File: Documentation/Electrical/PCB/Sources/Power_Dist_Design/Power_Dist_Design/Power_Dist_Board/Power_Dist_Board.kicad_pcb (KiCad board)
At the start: 2 copper layers, 150.5 x 84.8 mm, 59 parts, among them J1 Battery Connector, J2 +5V, J3 +5V, J4 +3.3V, J5 +3.3V, J6 GND, J7 GND, M1 Motor_DC, M10 Motor_DC, M2 Motor_DC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

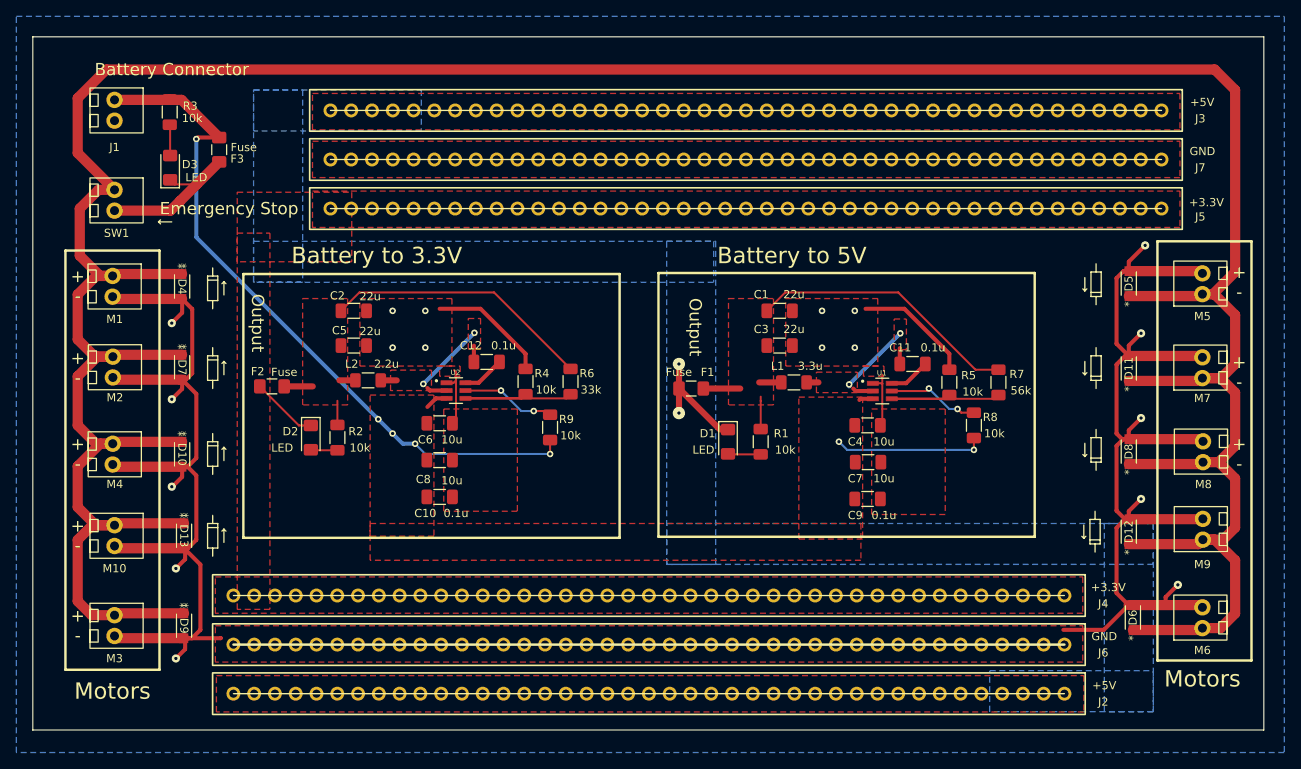
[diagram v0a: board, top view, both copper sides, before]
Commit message: Made final edits to pcb for ground isolation and EMI mitigation
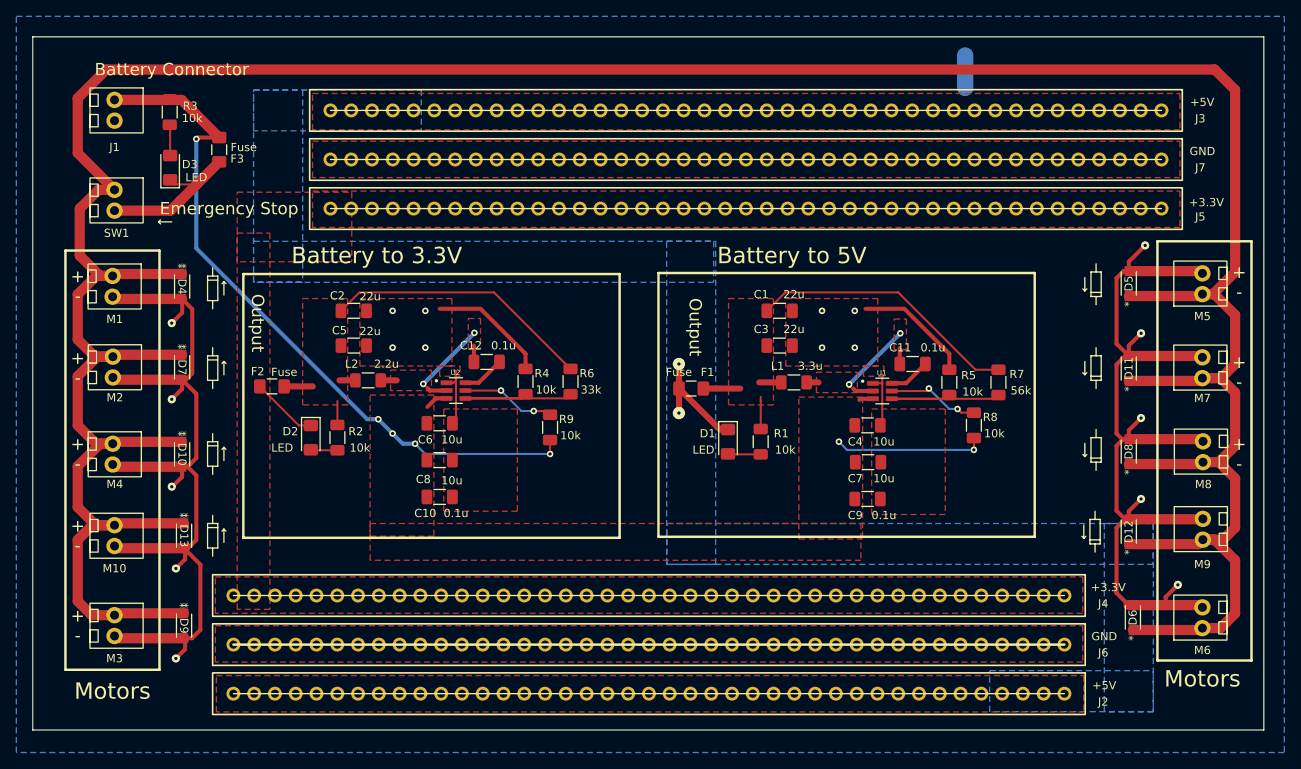
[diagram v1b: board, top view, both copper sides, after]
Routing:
- net GND: track 273.5 -> 264.3 mm
- net /vin: track 108.4 -> 109.2 mm
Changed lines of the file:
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@@
   )
   (dimension (type aligned) (layer "Eco1.User")
-    (pts (xy 239.5 20) (xy 239.5 104.5))
+    (pts (xy 235.75 20) (xy 235.75 104.5))
     (height -5.5)
-    (gr_text "3.3268 in" (at 243.85 62.25 90) (layer "Eco1.User")
+    (gr_text "84.5000 mm" (at 240.1 62.25 90) (layer "Eco1.User")
       (effects (font (size 1 1) (thickness 0.15)))
     )
@@
   )
   (dimension (type aligned) (layer "Eco1.User")
-    (pts (xy 82 113.5) (xy 232.5 113.5))
+    (pts (xy 82 108.25) (xy 232.5 108.25))
     (height 5)
-    (gr_text "5.9252 in" (at 157.25 117.35) (layer "Eco1.User")
+    (gr_text "150.5000 mm" (at 157.25 112.1) (layer "Eco1.User")
       (effects (font (size 1 1) (thickness 0.15)))
     )
@@
   (segment (start 214.5 60.065696) (end 215.544846 59.02085) (width 0.5) (layer "F.Cu") (net 2))
   (segment (start 100.633 93.633) (end 100.633 94.867) (width 0.5) (layer "F.Cu") (net 2))
-  (segment (start 215.976 89.476) (end 212.952 92.5) (width 0.5) (layer "F.Cu") (net 2))
-  (segment (start 212.952 92.5) (end 208 92.5) (width 0.5) (layer "F.Cu") (net 2))
   (segment (start 215.35375 48.64625) (end 216 48.64625) (width 0.5) (layer "F.Cu") (net 2))
   (segment (start 100.9375 72.5625) (end 102 73.625) (width 0.5) (layer "F.Cu") (net 2))
@@
   (segment (start 215.976 89.476) (end 214.5 88) (width 0.5) (layer "F.Cu") (net 2))
   (segment (start 100.633 83.867) (end 99.367 85.133) (width 0.5) (layer "F.Cu") (net 2))
-  (segment (start 101.024 93.524) (end 104.976 93.524) (width 0.5) (layer "F.Cu") (net 2))
   (segment (start 92.04 52.048) (end 91.766 51.774) (width 1.25) (layer "F.Cu") (net 2))
   (segment (start 184.7075 62.35375) (end 185.8125 62.35375) (width 0.25) (layer "F.Cu") (net 2))
-  (segment (start 104.976 93.524) (end 105 93.5) (width 0.5) (layer "F.Cu") (net 2))
   (segment (start 100.976 82.524) (end 100.5 82.524) (width 0.5) (layer "F.Cu") (net 2))
   (segment (start 100.9375 72.5625) (end 102 71.5) (width 0.5) (layer "F.Cu") (net 2))
@@
   (via (at 99.5 96) (size 1) (drill 0.4) (layers "F.Cu" "B.Cu") (net 2))
   (via (at 178.5 58) (size 0.8) (drill 0.4) (layers "F.Cu" "B.Cu") (free) (net 2))
+  (segment (start 196 22.28) (end 196 26.25) (width 2) (layer "B.Cu") (net 2))
   (segment (start 116 67.5125) (end 114.539 67.5125) (width 0.25) (layer "F.Cu") (net 3))
   (segment (start 109.7625 62.74) (end 109.7645 62.738) (width 0.5) (layer "F.Cu") (net 3))
@@
   (via (at 124.25 66.75) (size 0.8) (drill 0.4) (layers "F.Cu" "B.Cu") (net 4))
   (via (at 145.25 71) (size 0.8) (drill 0.4) (layers "F.Cu" "B.Cu") (net 4))
-  (segment (start 102 44.5) (end 124.25 66.75) (width 0.5) (layer "B.Cu") (net 4))
+  (segment (start 122.896446 66.75) (end 124.25 66.75) (width 0.5) (layer "B.Cu") (net 4))
   (segment (start 181.5625 70.5) (end 180.5625 69.5) (width 0.25) (layer "B.Cu") (net 4))
+  (segment (start 102 45.853554) (end 122.896446 66.75) (width 0.5) (layer "B.Cu") (net 4))
   (segment (start 145.25 71) (end 130 71) (width 0.25) (layer "B.Cu") (net 4))
-  (segment (start 102 32.5) (end 102 44.5) (width 0.5) (layer "B.Cu") (net 4))
   (segment (start 197.0625 70.5) (end 181.5625 70.5) (width 0.25) (layer "B.Cu") (net 4))
   (segment (start 126 68.5) (end 127.25 69.75) (width 0.5) (layer "B.Cu") (net 4))
   (segment (start 124.25 66.75) (end 126 68.5) (width 0.5) (layer "B.Cu") (net 4))
   (segment (start 130 71) (end 128.75 69.75) (width 0.25) (layer "B.Cu") (net 4))
+  (segment (start 102 32.5) (end 102 45.853554) (width 0.5) (layer "B.Cu") (net 4))
   (segment (start 127.25 69.75) (end 128.75 69.75) (width 0.5) (layer "B.Cu") (net 4))
   (segment (start 188 60) (end 188 58.0625) (width 0.5) (layer "F.Cu") (net 5))
@@
       )
     )
+  )
+  (zone (net 0) (net_name "") (layers "B.Cu" "Eco1.User") (hatch edge 0.5)
+    (connect_pads (clearance 0))
+    (min_thickness 0.25) (filled_areas_thickness no)
+    (keepout (tracks not_allowed) (vias allowed) (pads allowed) (copperpour not_allowed) (footprints allowed))
+    (fill (thermal_gap 0.5) (thermal_bridge_width 0.5))
+    (polygon
+      (pts
+        (xy 120 60.5)
+        (xy 125.5 60.5)
+        (xy 125.5 63.5)
+        (xy 120 63.5)
+      )
+    )
+  )
+  (zone (net 0) (net_name "") (layers "B.Cu" "Eco1.User") (hatch edge 0.5)
+    (connect_pads (clearance 0))
+    (min_thickness 0.25) (filled_areas_thickness no)
+    (keepout (tracks allowed) (vias allowed) (pads allowed) (copperpour not_allowed) (footprints allowed))
+    (fill (thermal_gap 0.5) (thermal_bridge_width 0.5))
+    (polygon
+      (pts
+        (xy 103 105)
+        (xy 105 105)
+        (xy 105 44)
+        (xy 103 44)
+      )
+    )
+  )
+  (zone (net 0) (net_name "") (layers "B.Cu" "Eco1.User") (hatch edge 0.5)
+    (connect_pads (clearance 0))
+    (min_thickness 0.25) (filled_areas_thickness no)
+    (keepout (tracks allowed) (vias allowed) (pads allowed) (copperpour not_allowed) (footprints allowed))
+    (fill (thermal_gap 0.5) (thermal_bridge_width 0.5))
+    (polygon
+      (pts
+        (xy 225 40)
+        (xy 225 38)
+        (xy 212 38)
+        (xy 212 40)
+      )
+    )
+  )
+  (zone (net 0) (net_name "") (layers "B.Cu" "Eco1.User") (hatch edge 0.5)
+    (connect_pads (clearance 0))
+    (min_thickness 0.25) (filled_areas_thickness no)
+    (keepout (tracks allowed) (vias allowed) (pads allowed) (copperpour not_allowed) (footprints allowed))
+    (fill (thermal_gap 0.5) (thermal_bridge_width 0.5))
+    (polygon
+      (pts
+        (xy 223 40)
+        (xy 225 40)
+        (xy 225 25)
+        (xy 223 25)
+      )
+    )
+  )
+  (zone (net 0) (net_name "") (layers "B.Cu" "Eco1.User") (hatch edge 0.5)
+    (connect_pads (clearance 0))
+    (min_thickness 0.25) (filled_areas_thickness no)
+    (keepout (tracks allowed) (vias allowed) (pads allowed) (copperpour not_allowed) (footprints allowed))
+    (fill (thermal_gap 0.5) (thermal_bridge_width 0.5))
+    (polygon
+      (pts
+        (xy 212 105)
+        (xy 214 105)
+        (xy 214 102.75)
+        (xy 212 102.75)
+      )
+    )
+  )
+  (zone (net 0) (net_name "") (layers "B.Cu" "Eco1.User") (hatch edge 0.5)
+    (connect_pads (clearance 0))
+    (min_thickness 0.25) (filled_areas_thickness no)
+    (keepout (tracks allowed) (vias allowed) (pads allowed) (copperpour not_allowed) (footprints allowed))
+    (fill (thermal_gap 0.5) (thermal_bridge_width 0.5))
+    (polygon
+      (pts
+        (xy 105 46)
+        (xy 105 44)
+        (xy 86 44)
+        (xy 86 46)
+      )
+    )
+  )
+  (zone (net 0) (net_name "") (layers "B.Cu" "Eco1.User") (hatch edge 0.5)
+    (connect_pads (clearance 0))
+    (min_thickness 0.25) (filled_areas_thickness no)
+    (keepout (tracks allowed) (vias allowed) (pads allowed) (copperpour not_allowed) (footprints allowed))
+    (fill (thermal_gap 0.5) (thermal_bridge_width 0.5))
+    (polygon
+      (pts
+        (xy 86 46)
+        (xy 88 46)
+        (xy 88 24)
+        (xy 86 24)
+      )
+    )
+  )
+  (zone (net 0) (net_name "") (layers "B.Cu" "Eco1.User") (hatch edge 0.5)
+    (connect_pads (clearance 0))
+    (min_thickness 0.25) (filled_areas_thickness no)
+    (keepout (tracks allowed) (vias allowed) (pads allowed) (copperpour not_allowed) (footprints allowed))
+    (fill (thermal_gap 0.5) (thermal_bridge_width 0.5))
+    (polygon
+      (pts
+        (xy 225 26)
+        (xy 225 24)
+        (xy 87 24)
+        (xy 87 26)
+      )
+    )
+  )
+  (zone (net 0) (net_name "") (layers "B.Cu" "Eco1.User") (hatch edge 0.5)
+    (connect_pads (clearance 0))
+    (min_thickness 0.25) (filled_areas_thickness no)
+    (keepout (tracks not_allowed) (vias allowed) (pads allowed) (copperpour not_allowed) (footprints allowed))
+    (fill (thermal_gap 0.5) (thermal_bridge_width 0.5))
+    (polygon
+      (pts
+        (xy 172.25 60.75)
+        (xy 177.75 60.75)
+        (xy 177.75 63.75)
+        (xy 172.25 63.75)
+      )
+    )
+  )
+  (zone (net 0) (net_name "") (layers "B.Cu" "Eco1.User") (hatch edge 0.5)
+    (connect_pads (clearance 0))
+    (min_thickness 0.25) (filled_areas_thickness no)
+    (keepout (tracks allowed) (vias allowed) (pads allowed) (copperpour not_allowed) (footprints allowed))
+    (fill (thermal_gap 0.5) (thermal_bridge_width 0.5))
+    (polygon
+      (pts
+        (xy 212 79.25)
+        (xy 214 79.25)
+        (xy 214 38)
+        (xy 212 38)
+      )
+    )
